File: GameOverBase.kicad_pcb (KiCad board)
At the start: 4 copper layers, 50 x 35 mm, 47 parts, among them J1 USB_C_DEALON-USB-US31-106, J2 Serial Port, J3 add-on conn, Q1 PMN48XP, SW1 SW_DIP_x08, SW2 boot, SW3 Reset, U1 ESP32-WROOM-E, U2 4021, U3 MCP73831-2ACI-OT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

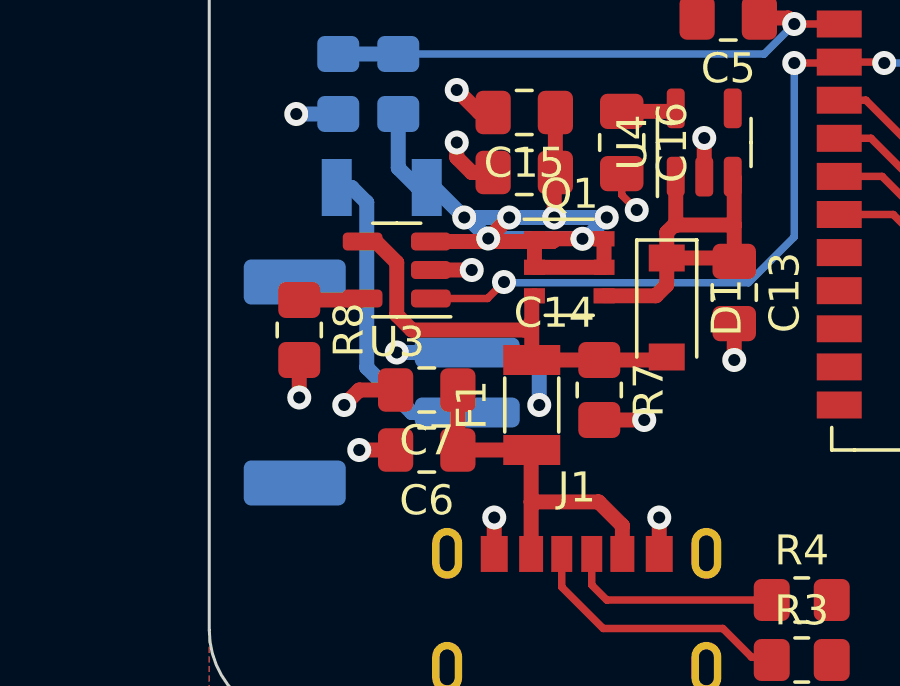
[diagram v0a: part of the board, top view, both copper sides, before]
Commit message: Moves battery connector further in the board
This will allow the cable to fit better inside the enclosure
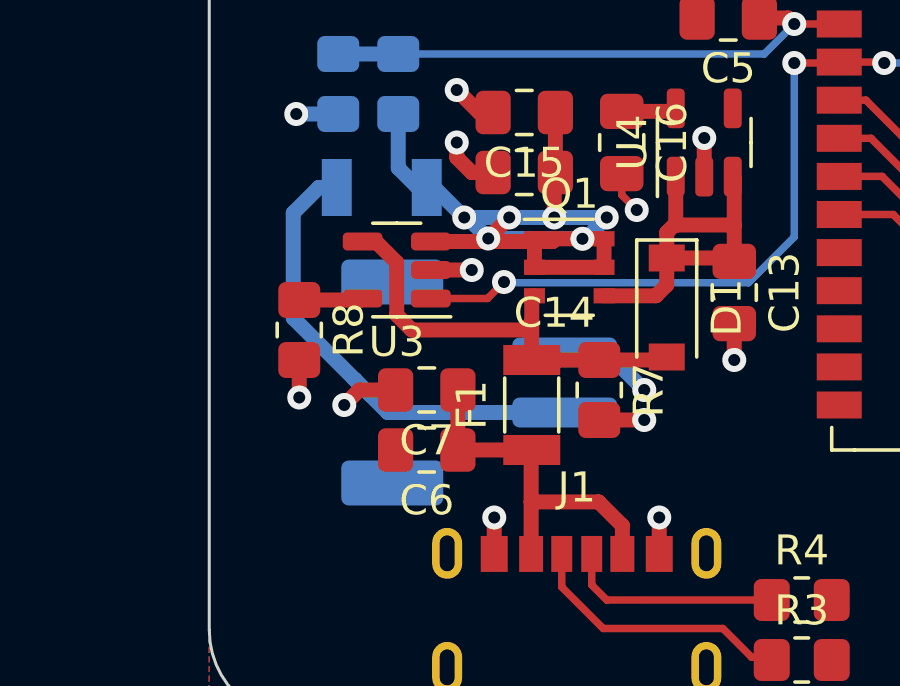
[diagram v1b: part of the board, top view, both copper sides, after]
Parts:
- moved BT1 3.25 mm to (129.0, 103.8)
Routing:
- net Net-(BT1-+): track 10.7 -> 15.7 mm
- net GND: track 86.5 -> 82.2 mm, vias 36 -> 34
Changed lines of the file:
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@@
   )
   (footprint "Connector_JST:JST_PH_S2B-PH-SM4-TB_1x02-1MP_P2.00mm_Horizontal" (layer "B.Cu")
-    (at 125.75 103.75 90)
+    (at 129 103.75 90)
     (descr "JST PH series connector, S2B-PH-SM4-TB (http://www.jst-mfg.com/product/pdf/eng/ePH.pdf), generated with kicad-footprint-generator")
     (tags "connector JST PH top entry")
@@
   (gr_arc (start 167 80) (mid 169.12132 80.87868) (end 170 83)
     (stroke (width 0.1) (type default)) (layer "Edge.Cuts"))
-  (segment (start 128.6 104.75) (end 126.75 104.75) (width 0.5) (layer "B.Cu") (net 1))
-  (segment (start 125.25 103.25) (end 125.25 97.75) (width 0.5) (layer "B.Cu") (net 1))
-  (segment (start 125.25 97.75) (end 124.75 97.25) (width 0.5) (layer "B.Cu") (net 1))
-  (segment (start 124.75 97.25) (end 124.25 97.25) (width 0.5) (layer "B.Cu") (net 1))
-  (segment (start 126.75 104.75) (end 125.25 103.25) (width 0.5) (layer "B.Cu") (net 1))
+  (segment (start 122.8 98.1) (end 123.65 97.25) (width 0.5) (layer "B.Cu") (net 1))
+  (segment (start 125.349511 104.149511) (end 125.349511 104.14812) (width 0.5) (layer "B.Cu") (net 1))
+  (segment (start 125.95 104.75) (end 125.349511 104.149511) (width 0.5) (layer "B.Cu") (net 1))
+  (segment (start 131.85 104.75) (end 125.95 104.75) (width 0.5) (layer "B.Cu") (net 1))
+  (segment (start 123.65 97.25) (end 124.25 97.25) (width 0.5) (layer "B.Cu") (net 1))
+  (segment (start 124.850489 103.650489) (end 122.8 101.6) (width 0.5) (layer "B.Cu") (net 1))
+  (segment (start 122.8 101.6) (end 122.8 98.1) (width 0.5) (layer "B.Cu") (net 1))
+  (segment (start 125.349511 104.14812) (end 124.85188 103.650489) (width 0.5) (layer "B.Cu") (net 1))
+  (segment (start 124.85188 103.650489) (end 124.850489 103.650489) (width 0.5) (layer "B.Cu") (net 1))
   (segment (start 136.7 87.1625) (end 136.7 86) (width 0.5) (layer "F.Cu") (net 2))
   (segment (start 163.15 97.46) (end 163.95 97.46) (width 0.25) (layer "F.Cu") (net 2))
@@
   (segment (start 147.545 95.33) (end 146.08 95.33) (width 0.5) (layer "F.Cu") (net 2))
   (segment (start 147.545 95.33) (end 147.545 93.805) (width 0.5) (layer "F.Cu") (net 2))
-  (segment (start 126.2125 106) (end 125 106) (width 0.5) (layer "F.Cu") (net 2))
   (segment (start 147.545 96.855) (end 147.545 95.33) (width 0.5) (layer "F.Cu") (net 2))
   (segment (start 147.545 96.855) (end 146.105 96.855) (width 0.5) (layer "F.Cu") (net 2))
@@
   (via (at 159.805378 88.094622) (size 0.8) (drill 0.4) (layers "F.Cu" "B.Cu") (net 2))
   (via (at 149.05 92.4) (size 0.8) (drill 0.4) (layers "F.Cu" "B.Cu") (net 2))
-  (via (at 125 106) (size 0.8) (drill 0.4) (layers "F.Cu" "B.Cu") (net 2))
   (via (at 137.5 103) (size 0.8) (drill 0.4) (layers "F.Cu" "B.Cu") (net 2))
   (via (at 124.5 104.5) (size 0.8) (drill 0.4) (layers "F.Cu" "B.Cu") (net 2))
@@
   (via (at 123 104.25) (size 0.8) (drill 0.4) (layers "F.Cu" "B.Cu") (net 2))
   (via (at 142.5 88.01) (size 0.8) (drill 0.4) (layers "F.Cu" "B.Cu") (net 2))
-  (via (at 126.25 102.75) (size 0.8) (drill 0.4) (layers "F.Cu" "B.Cu") (net 2))
   (via (at 151.95 93.8) (size 0.8) (drill 0.4) (layers "F.Cu" "B.Cu") (net 2))
   (via (at 164.2 94.21) (size 0.8) (drill 0.4) (layers "F.Cu" "B.Cu") (net 2))
@@
   (via (at 128.25 94) (size 0.8) (drill 0.4) (layers "F.Cu" "B.Cu") (net 2))
   (via (at 146.05 95.3) (size 0.8) (drill 0.4) (layers "F.Cu" "B.Cu") (net 2))
+  (via (at 134.5 104) (size 0.8) (drill 0.4) (layers "F.Cu" "B.Cu") (net 2))
   (via (at 150.55 98.2) (size 0.8) (drill 0.4) (layers "F.Cu" "B.Cu") (net 2))
   (via (at 151.95 96.8) (size 0.8) (drill 0.4) (layers "F.Cu" "B.Cu") (net 2))
@@
   (via (at 150.55 92.4) (size 0.8) (drill 0.4) (layers "F.Cu" "B.Cu") (net 2))
   (via (at 161.9 106.21) (size 0.8) (drill 0.4) (layers "F.Cu" "B.Cu") (net 2))
-  (via (at 131 104.5) (size 0.8) (drill 0.4) (layers "F.Cu" "B.Cu") (net 2))
   (via (at 146.05 93.8) (size 0.8) (drill 0.4) (layers "F.Cu" "B.Cu") (net 2))
   (via (at 136.5 95.6) (size 0.8) (drill 0.4) (layers "F.Cu" "B.Cu") (net 2))
   (via (at 144 104.15) (size 0.8) (drill 0.4) (layers "F.Cu" "B.Cu") (net 2))
   (segment (start 161.9 107.0375) (end 162.0625 107.2) (width 0.25) (layer "B.Cu") (net 2))
-  (segment (start 130.5 102.75) (end 128.6 102.75) (width 0.5) (layer "B.Cu") (net 2))
   (segment (start 164.9 98.7) (end 165.8625 98.7) (width 0.25) (layer "B.Cu") (net 2))
   (segment (start 164.9 96.51) (end 164.9 95.61) (width 0.25) (layer "B.Cu") (net 2))
-  (segment (start 131 103.25) (end 130.5 102.75) (width 0.5) (layer "B.Cu") (net 2))
   (segment (start 164.9 95.61) (end 165.1375 95.3725) (width 0.25) (layer "B.Cu") (net 2))
   (segment (start 165.8625 98.7) (end 165.9 98.6625) (width 0.25) (layer "B.Cu") (net 2))
   (segment (start 164.2 94.21) (end 164.2 92.6725) (width 0.25) (layer "B.Cu") (net 2))
-  (segment (start 126.25 102.75) (end 128.6 102.75) (width 0.5) (layer "B.Cu") (net 2))
   (segment (start 161.9 106.21) (end 161.9 107.5475) (width 0.25) (layer "B.Cu") (net 2))
+  (segment (start 131.85 102.75) (end 133.25 102.75) (width 0.5) (layer "B.Cu") (net 2))
   (segment (start 164.6 99) (end 164.9 98.7) (width 0.25) (layer "B.Cu") (net 2))
   (segment (start 164.5 96.91) (end 164.9 96.51) (width 0.25) (layer "B.Cu") (net 2))
-  (segment (start 131 104.5) (end 131 103.25) (width 0.5) (layer "B.Cu") (net 2))
+  (segment (start 133.25 102.75) (end 134.5 104) (width 0.5) (layer "B.Cu") (net 2))
   (segment (start 124.3 94.8) (end 122.9 94.8) (width 0.5) (layer "B.Cu") (net 2))
   (segment (start 165.1375 94.8625) (end 165.9 94.8625) (width 0.25) (layer "B.Cu") (net 2))

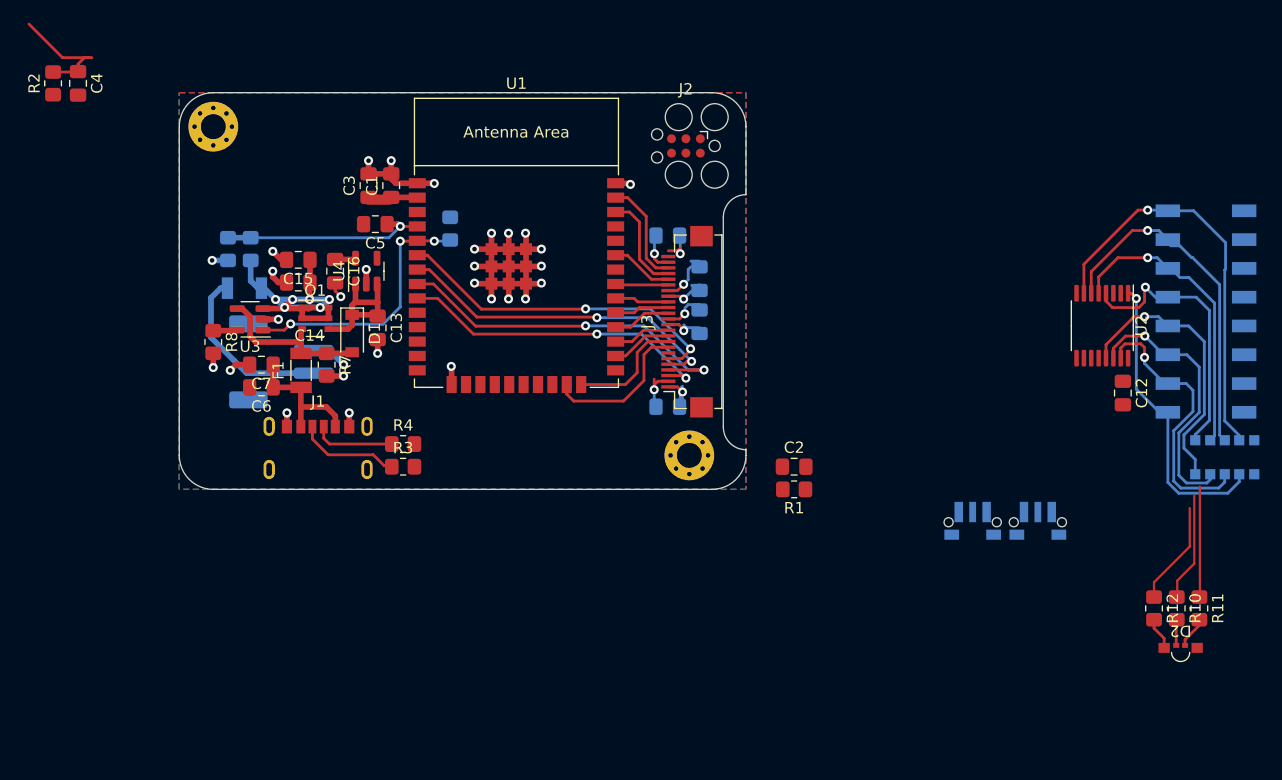
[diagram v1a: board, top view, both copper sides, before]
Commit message: Adds resistors and capacitors for ESP enable and boot pins
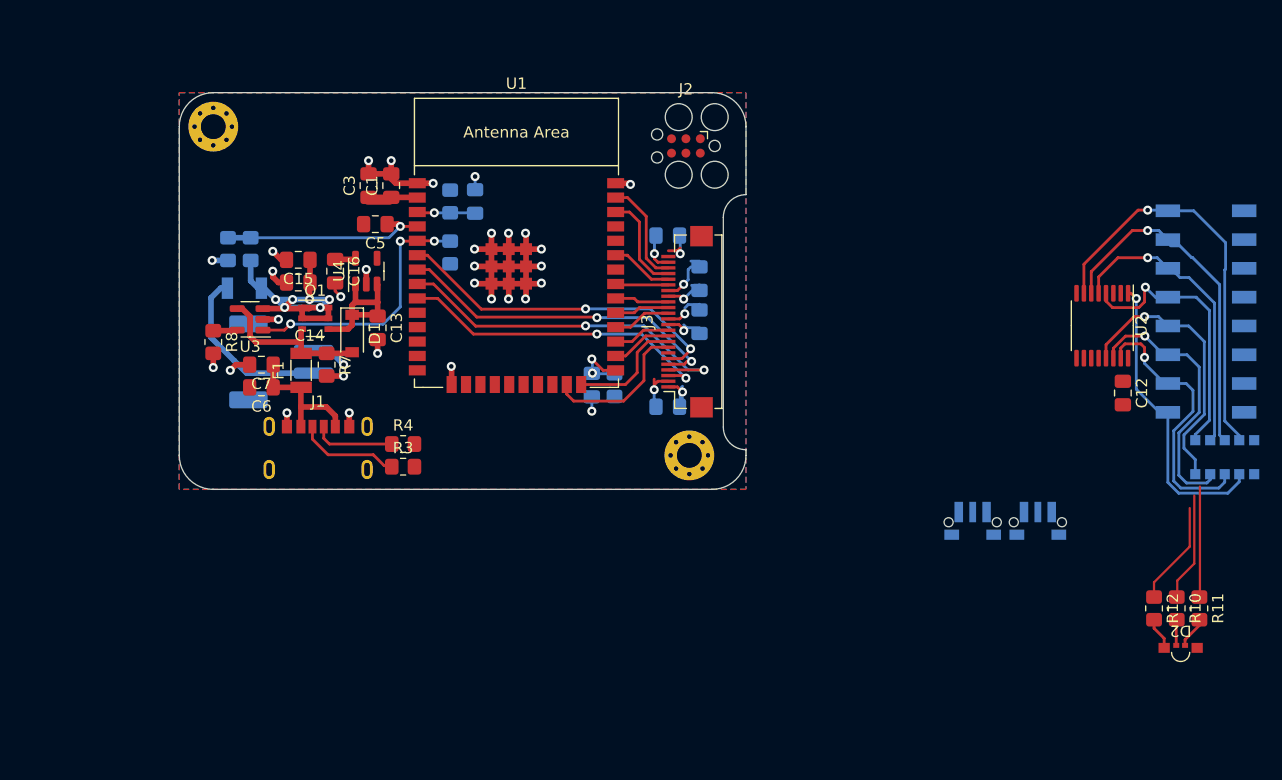
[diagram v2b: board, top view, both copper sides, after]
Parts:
- C2, C4, R1, R2: moved to B.Cu
- moved R2 36.5 mm to (143.9, 89.6), turned to -90 degrees
- moved C4 36.5 mm to (146.1, 89.6), turned to 90 degrees
- moved C2 19.2 mm to (156.4, 105.8), turned to -90 degrees
- moved R1 18.3 mm to (158.4, 105.8), turned to 90 degrees
- moved R9 2.10 mm to (143.9, 94.1), turned to 90 degrees
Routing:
- net ESP_BOOT: track 0.00 -> 5.75 mm, vias 0 -> 2
- net ESP_EN: track 10.9 -> 5.14 mm, vias 0 -> 1
- net GND: track 82.2 -> 84.5 mm, vias 34 -> 36
